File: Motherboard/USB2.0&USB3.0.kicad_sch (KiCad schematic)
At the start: 27 parts, among them J4 USB3_A_Stacked, J5 USB_A_Stacked, J79 Conn_01x04_Socket, J80 Conn_01x04_Socket, U3 ULC0524P, U4 ULC0524P, U5 ULC0524P, U78 ULC0524P

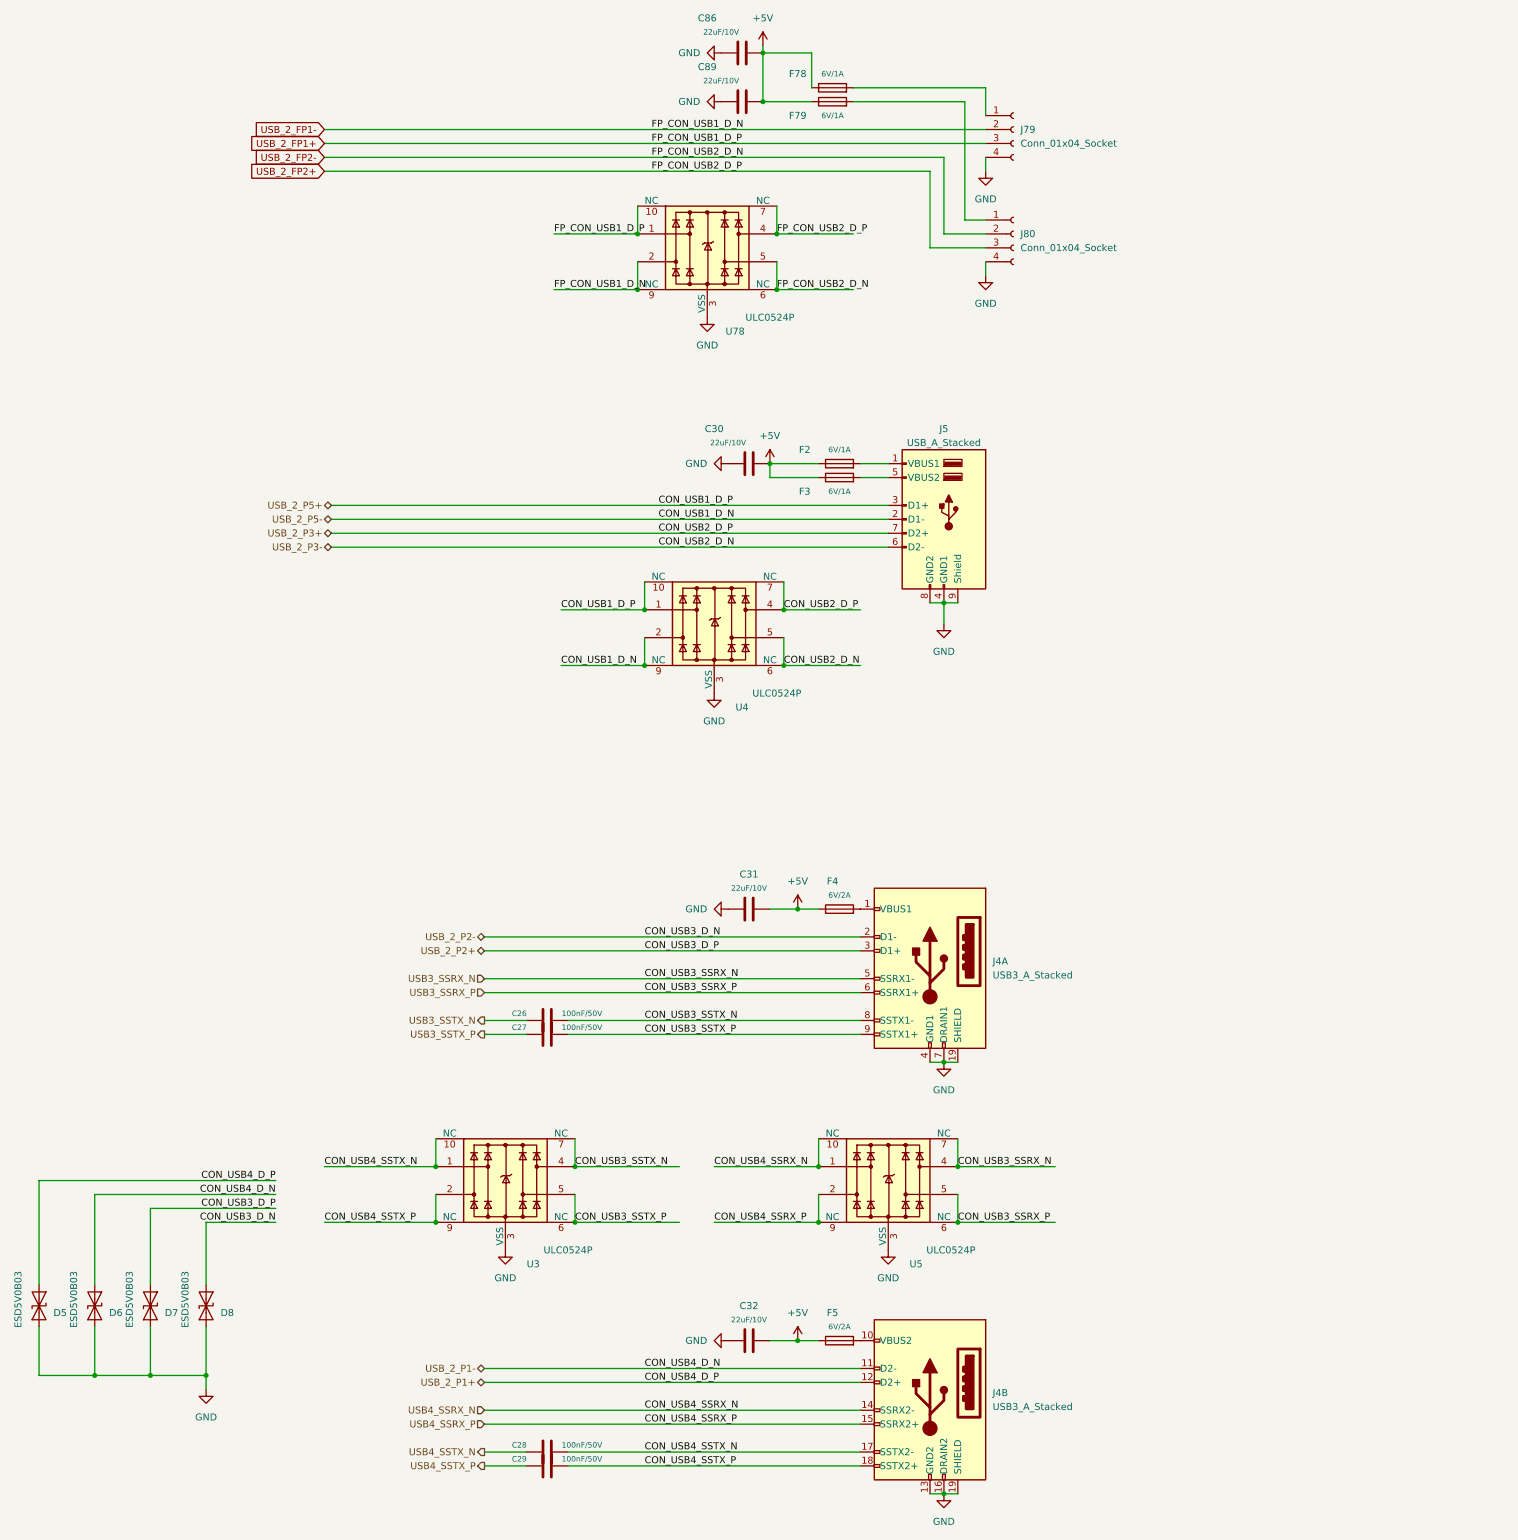
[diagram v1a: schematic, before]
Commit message: Added RP2040 MCU, Handles all External IO Systems (Except Audio), WIP.
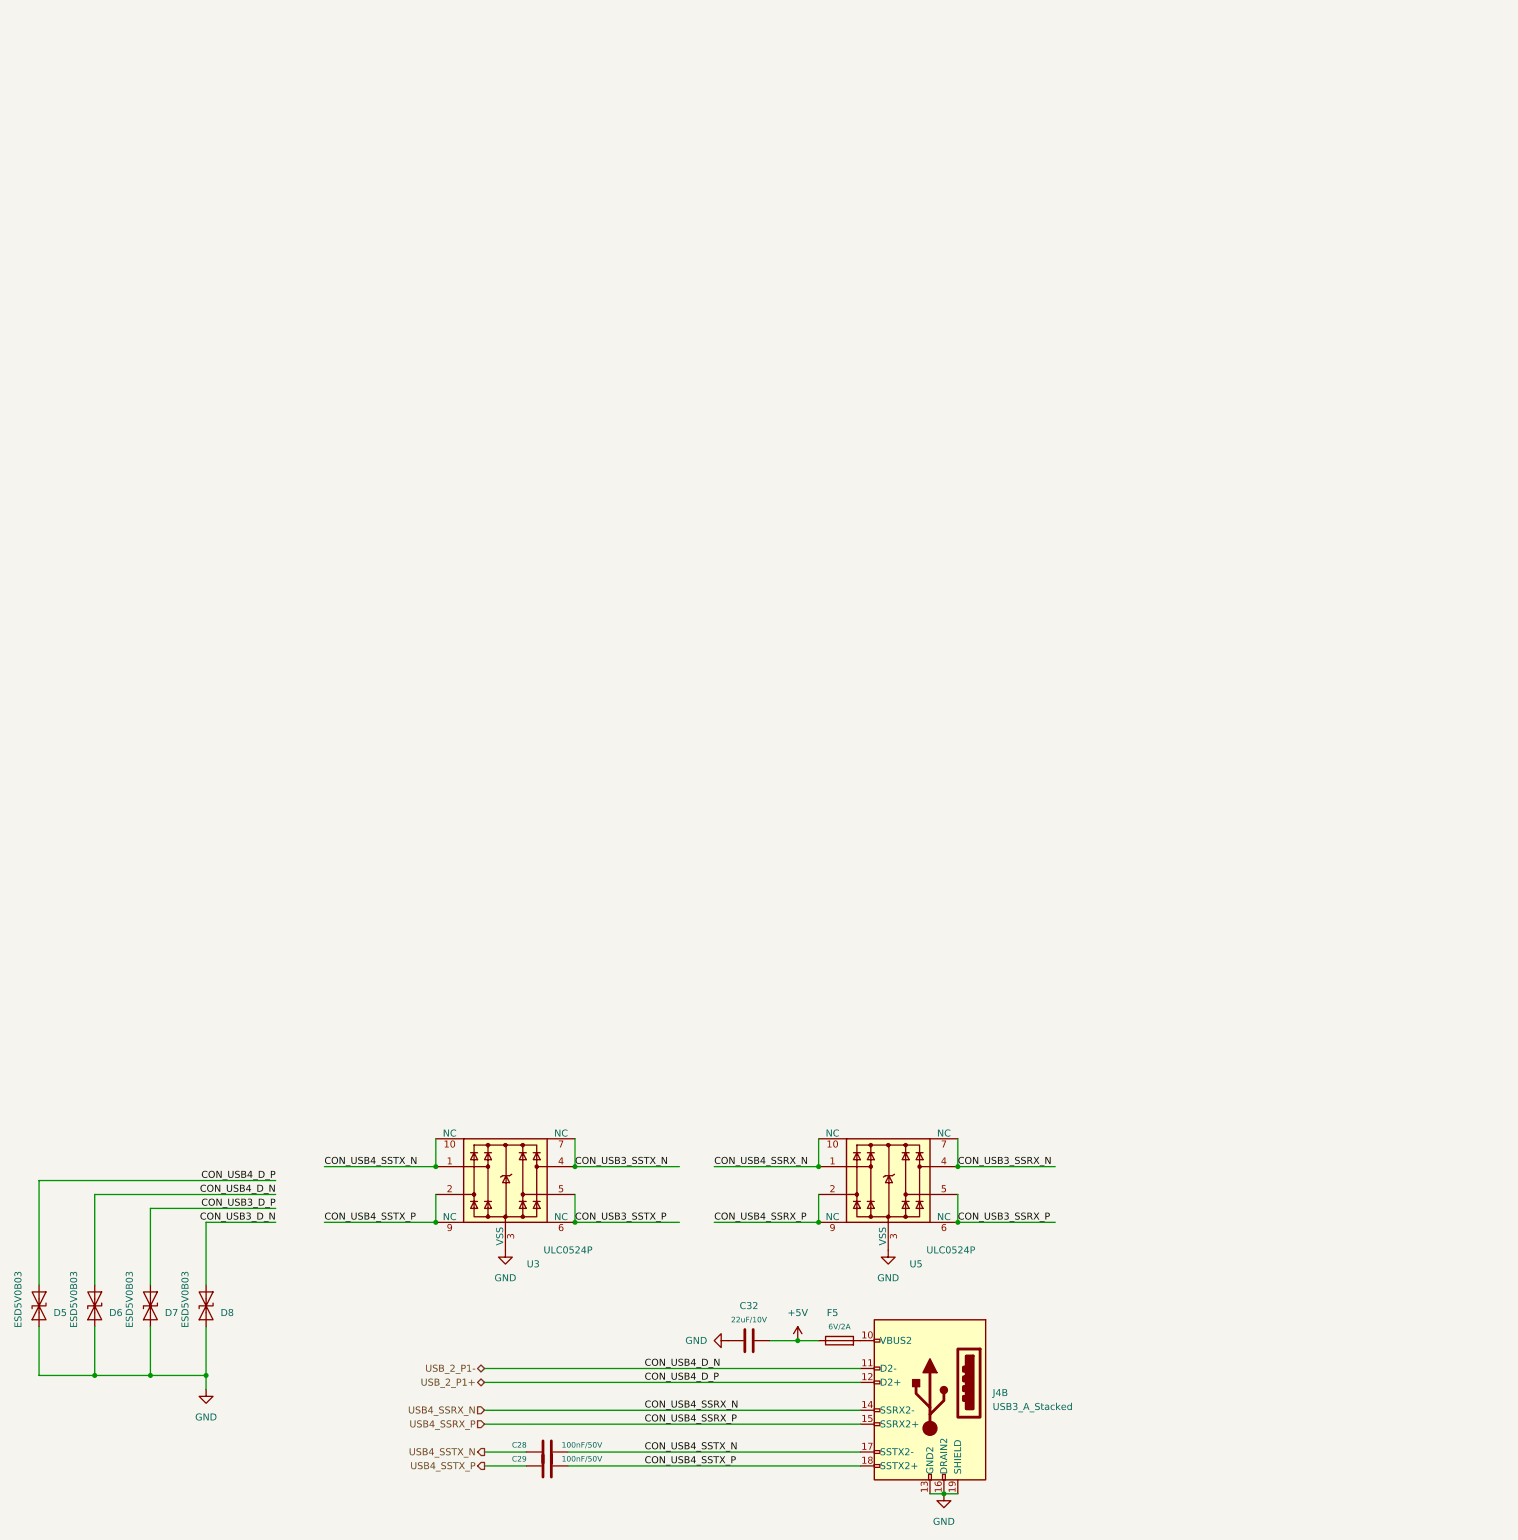
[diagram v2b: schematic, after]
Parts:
- removed C26, C27: 100nF/50V, A_HDJ_Library:C_0402_1005Metric, symbol Device:C
- removed C30, C31, C86, C89: 22uF/10V, A_HDJ_Library:C_0603_1608Metric, symbol Device:C
- removed F2, F3, F78, F79: 6V/1A, A_HDJ_Library:Fuse_0805_2012Metric, symbol Device:Fuse
- removed F4: 6V/2A, A_HDJ_Library:R_0805_2012Metric, symbol Device:Fuse
- removed unit 1 of J4
- removed J5: USB_A_Stacked, A_HDJ_Library:USB_A_CUI_UJ2-ADH-TH_Horizontal_Stacked, symbol Connector:USB_A_Stacked
- removed J79, J80: Conn_01x04_Socket, Connector_JST:JST_XH_B4B-XH-A_1x04_P2.50mm_Vertical, symbol Connector:Conn_01x04_Socket
- removed U4, U78: ULC0524P, A_HDJ_Library:Diodes_UDFN-10_1.0x2.5mm_P0.5mm, symbol Power_Protection:D3V3XA4B10LP
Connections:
- net USB3_SSRX_N renamed CON_USB3_SSRX_N
- net USB3_SSRX_P renamed CON_USB3_SSRX_P
- net USB_2_P2+ renamed CON_USB3_D_P
- net USB_2_P2- renamed CON_USB3_D_N

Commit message: Motherboard Complete (aside from parts-BOM associations)
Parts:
- removed C28, C29: 100nF/50V, A_HDJ_Library:C_0402_1005Metric, symbol Device:C
- removed C32: 22uF/10V, A_HDJ_Library:C_0603_1608Metric, symbol Device:C
- removed D5, D6: ESD5V0B03, A_HDJ_Library:D_0402_1005Metric, symbol Diode:ESD9B5.0ST5G
- removed F5: 6V/2A, A_HDJ_Library:Fuse_0805_2012Metric, symbol Device:Fuse
- added C26, C27, C30, C31: 100nF/50V, A_HDJ_Library:C_0402_1005Metric, symbol Device:C
- added C62, C63, C86: 22uF/10V, A_HDJ_Library:C_0603_1608Metric, symbol Device:C
- added D15, D16: ESD5V0B03, A_HDJ_Library:D_0402_1005Metric, symbol Diode:ESD9B5.0ST5G
- added F3: 6V/1A, A_HDJ_Library:Fuse_0805_2012Metric, symbol Device:Fuse
- added F4: 6V/2A, A_HDJ_Library:R_0805_2012Metric, symbol Device:Fuse
- added F6: 6V/2A, A_HDJ_Library:Fuse_0805_2012Metric, symbol Device:Fuse
- added unit 1 of J4
- added J81: USB_A, symbol Connector:USB_A
- added U9: ULC0524P, A_HDJ_Library:Diodes_UDFN-10_1.0x2.5mm_P0.5mm, symbol Power_Protection:D3V3XA4B10LP
- U5: now not fitted; now left out of the parts list
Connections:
- net CON_USB3_D_N is gone; now on net USB_2_P1-: D8.2 (A2)
- net CON_USB3_D_P is gone; now on net USB_2_P1+: D7.2 (A2)
- net +5V: now also C62.2, C63.2, C86.2, F3.1, F4.1, F6.1
- net CON_USB3_SSTX_N: now also C26.2, J4.8 (SSTX1-)
- net CON_USB3_SSTX_P: now also C27.2, J4.9 (SSTX1+)
- net CON_USB4_SSTX_N: now also C30.2
- net CON_USB4_SSTX_P: now also C31.2
- net GND: now also C62.1, C63.1, C86.1, D15.1 (A1), D16.1 (A1), J4.19 (SHIELD), J4.4 (GND1), J4.7 (DRAIN1), J81.4 (GND), J81.SH (Shield), U9.3 (VSS), U9.8 (VSS)
- net USB4_SSRX_N: now also U9.1, U9.10 (NC); no longer U5.1, U5.10 (NC)
- net USB4_SSRX_P: now also U9.2, U9.9 (NC); no longer U5.2, U5.9 (NC)
- net USB4_SSTX_N: now also C30.1
- net USB4_SSTX_P: now also C31.1
- net at J4.10 (VBUS2): now also F6.2
- net CON_USB3_SSRX_N: no longer names the net of U5.4, U5.7 (NC)
- net CON_USB3_SSRX_P: no longer names the net of U5.5, U5.6 (NC)
- new net: F4.2, J4.1 (VBUS1)
- new net: F3.2, J81.1 (VBUS)
- new net USB3_SSRX_N: J4.5 (SSRX1-), U9.4, U9.7 (NC)
- new net USB3_SSRX_P: J4.6 (SSRX1+), U9.5, U9.6 (NC)
- new net USB3_SSTX_N: C26.1
- new net USB3_SSTX_P: C27.1
- new net USB_2_P2+: D15.2 (A2), J4.3 (D1+)
- new net USB_2_P2-: D16.2 (A2), J4.2 (D1-)
- new net USB_2_P3+: J81.3 (D+), U5.1, U5.10 (NC)
- new net USB_2_P3-: J81.2 (D-), U5.2, U5.9 (NC)

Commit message: Removed CTRL_L_SLI as it is no longer used. Switched MCU from RP2040 to RP2354B, for the added ADC inputs.
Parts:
- added J82, J92: USB3_A, Connector_USB:USB3_A_Molex_48393-001, symbol Connector:USB3_A
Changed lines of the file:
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@@
+	)
+	(symbol
+		(lib_id "Connector:USB3_A")
+		(at 402.59 189.23 0)
+		(mirror y)
+		(unit 1)
+		(body_style 1)
+		(exclude_from_sim no)
+		(in_bom yes)
+		(on_board yes)
+		(in_pos_files yes)
+		(dnp no)
+		(fields_autoplaced yes)
+		(property "Reference" "J82"
+			(at 414.02 188.5949 0)
+			(show_name no)
+			(do_not_autoplace no)
+			(effects
+				(font
+					(size 1.27 1.27)
+				)
+				(justify right)
+			)
+		)
+		(property "Value" "USB3_A"
+			(at 414.02 191.1349 0)
+			(show_name no)
+			(do_not_autoplace no)
+			(effects
+				(font
+					(size 1.27 1.27)
+				)
+				(justify right)
+			)
+		)
+		(property "Footprint" "Connector_USB:USB3_A_Molex_48393-001"
+			(at 398.78 186.69 0)
+			(hide yes)
+			(show_name no)
+			(do_not_autoplace no)
+			(effects
+				(font
+					(size 1.27 1.27)
+				)
+			)
+		)
+		(property "Datasheet" ""
+			(at 398.78 186.69 0)
+			(hide yes)
+			(show_name no)
+			(do_not_autoplace no)
+			(effects
+				(font
+					(size 1.27 1.27)
+				)
+			)
+		)
+		(property "Description" "USB 3.0 A connector"
+			(at 402.59 189.23 0)
+			(hide yes)
+			(show_name no)
+			(do_not_autoplace no)
+			(effects
+				(font
+					(size 1.27 1.27)
+				)
+			)
+		)
+		(pin "8"
+		)
+		(pin "1"
+		)
+		(pin "3"
+		)
+		(pin "4"
+		)
+		(pin "5"
+		)
+		(pin "6"
+		)
+		(pin "2"
+		)
+		(pin "7"
+		)
+		(pin "SH"
+		)
+		(pin "9"
+		)
+		(instances
+			(project "Motherboard"
+				(path "/2a6d114a-7fd7-4207-b5f7-4ea9c34f36aa/f9aa04f2-8362-4e9f-9e54-e2b1a8ec9b0a"
+					(reference "J82")
+					(unit 1)
+				)
+			)
+		)
 	)
 	(symbol
@@
 					(unit 1)
 				)
+			)
+		)
+	)
+	(symbol
+		(lib_id "Connector:USB3_A")
+		(at 402.59 267.97 0)
+		(mirror y)
+		(unit 1)
+		(body_style 1)
+		(exclude_from_sim no)
+		(in_bom yes)
+		(on_board yes)
+		(in_pos_files yes)
+		(dnp no)
+		(fields_autoplaced yes)
+		(property "Reference" "J92"
+			(at 414.02 267.3349 0)
+			(show_name no)
+			(do_not_autoplace no)
+			(effects
+				(font
+					(size 1.27 1.27)
+				)
+				(justify right)
+			)
+		)
+		(property "Value" "USB3_A"
+			(at 414.02 269.8749 0)
+			(show_name no)
+			(do_not_autoplace no)
+			(effects
+				(font
+					(size 1.27 1.27)
+				)
+				(justify right)
+			)
+		)
+		(property "Footprint" "Connector_USB:USB3_A_Molex_48393-001"
+			(at 398.78 265.43 0)
+			(hide yes)
+			(show_name no)
+			(do_not_autoplace no)
+			(effects
+				(font
+					(size 1.27 1.27)
+				)
+			)
+		)
+		(property "Datasheet" ""
+			(at 398.78 265.43 0)
+			(hide yes)
+			(show_name no)
+			(do_not_autoplace no)
+			(effects
+				(font
+					(size 1.27 1.27)
+				)
+			)
+		)
+		(property "Description" "USB 3.0 A connector"
+			(at 402.59 267.97 0)
+			(hide yes)
+			(show_name no)
+			(do_not_autoplace no)
+			(effects
+				(font
+					(size 1.27 1.27)
+				)
+			)
+		)
+		(pin "8"
+		)
+		(pin "1"
+		)
+		(pin "3"
+		)
+		(pin "4"
+		)
+		(pin "5"
+		)
+		(pin "6"
+		)
+		(pin "2"
+		)
+		(pin "7"
+		)
+		(pin "SH"
+		)
+		(pin "9"
+		)
+		(instances
+			(project "Motherboard"
+				(path "/2a6d114a-7fd7-4207-b5f7-4ea9c34f36aa/f9aa04f2-8362-4e9f-9e54-e2b1a8ec9b0a"
+					(reference "J92")
+					(unit 1)
+				)
